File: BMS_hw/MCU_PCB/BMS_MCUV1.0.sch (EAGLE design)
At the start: 49 parts, among them IC2 SST25VF020B804ISA, J1 22-27-2051-05, J2 22-27-2051-05, J3 22-27-2041-04, J4 22-27-2051-05, U1 NCP1117LP-PG, X1 87758-2016

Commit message: Testing git bash trial !
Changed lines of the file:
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@@
 </instance>
 <instance part="X3" gate="-10" x="109.22" y="231.14" rot="R180">
-<attribute name="NAME" x="106.68" y="231.902" size="1.524" layer="95" rot="R180"/>
+<attribute name="NAME" x="99.06" y="236.982" size="1.524" layer="95" rot="R180"/>
 </instance>
 </instances>

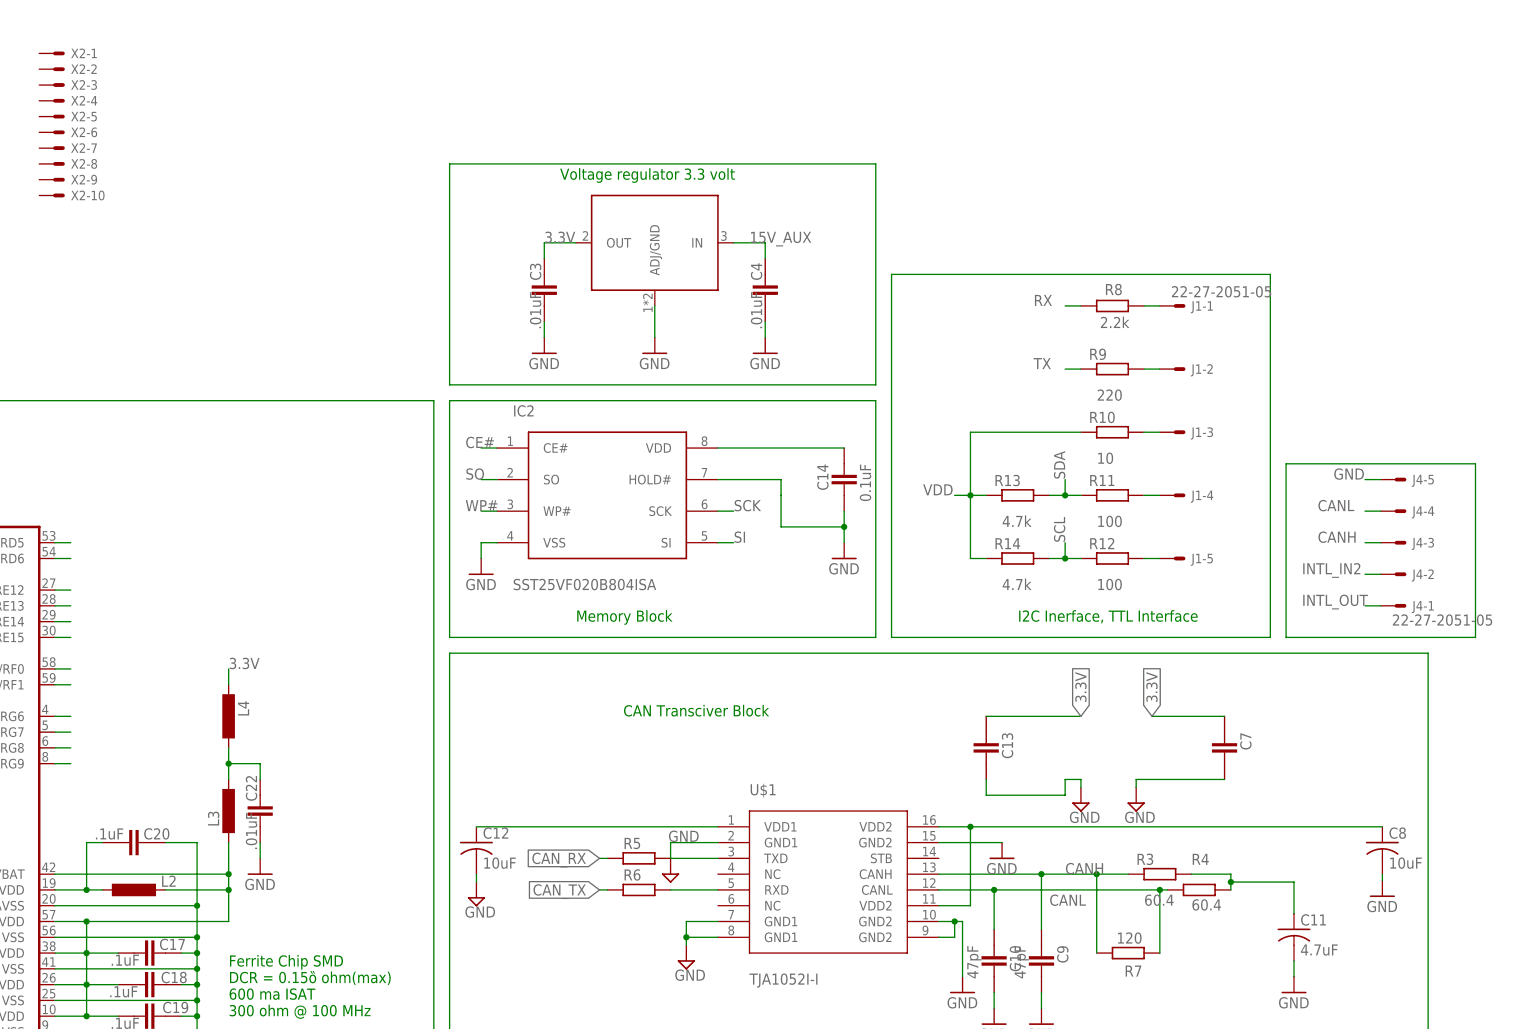
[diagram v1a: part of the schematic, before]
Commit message: updated schematic inductor part no 3.3 5v ldo net naaming
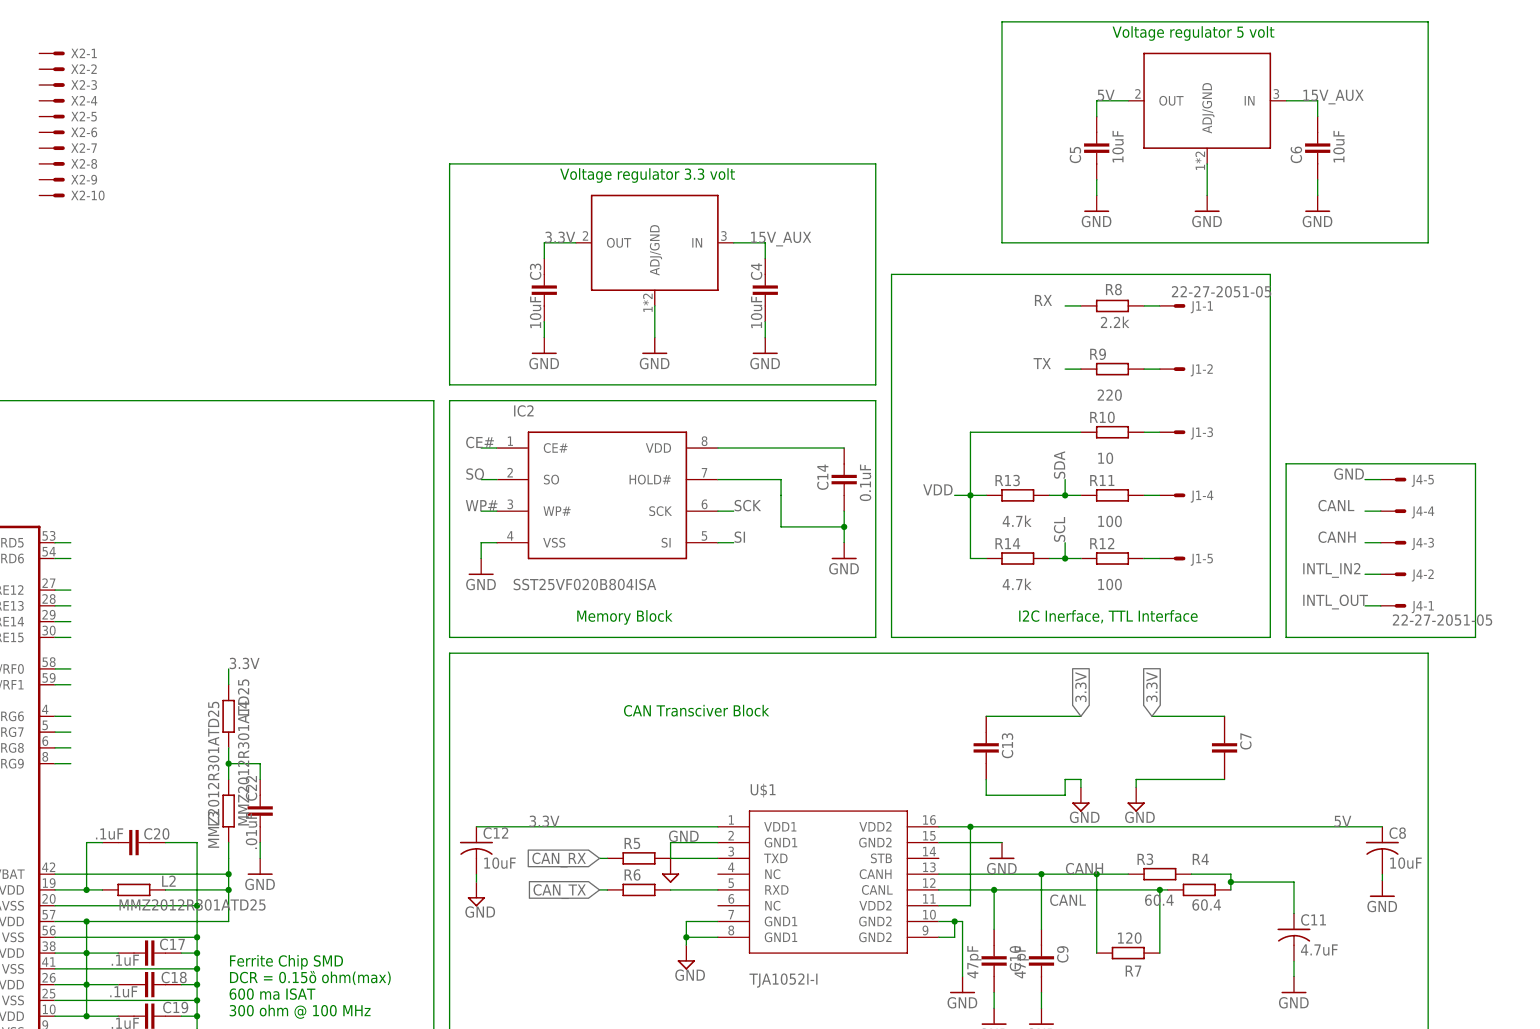
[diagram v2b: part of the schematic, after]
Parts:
- added C5, C6: 10uF, ipc-7351-capacitor:CAPACITOR_0603
- added U2: NCP1117LP-PG, GreenFuel:NCP1117LP-PG
- C3, C4: value .01uF -> 10uF
- L2, L3, L4: value (none) -> MMZ2012R301ATD25; device ipc-7351-inductor:INDUCTOR_0603 -> ipc-7351-resistor:RESISTOR_0805
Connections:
- removed net N$12: C8.1, U$1.VDD2, U$1.VDD2@1
- removed net N$8: C12.1, U$1.VDD1
- new net 5V: C5.2, C8.1, U$1.VDD2, U$1.VDD2@1, U2.OUT
- net 15V_AUX: now also C6.2, U2.IN
- net 3.3V: now also C12.1, U$1.VDD1
- net GND: now also C5.1, C6.1, U2.ADJ/GND
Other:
- note added: "Voltage regulator 5 volt"
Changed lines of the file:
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@@
 <part name="C19" library="ipc-7351-capacitor" deviceset="CAPACITOR_" device="0603" value=".1uF"/>
 <part name="GND21" library="supply1" library_urn="urn:adsk.eagle:library:371" deviceset="GND" device=""/>
-<part name="L2" library="ipc-7351-inductor" deviceset="INDUCTOR_" device="0603"/>
+<part name="L2" library="ipc-7351-resistor" deviceset="RESISTOR_" device="0805" value="MMZ2012R301ATD25"/>
 <part name="C20" library="ipc-7351-capacitor" deviceset="CAPACITOR_" device="0603" value=".1uF"/>
 <part name="R15" library="ipc-7351-resistor" deviceset="RESISTOR_" device="0603" value="1k"/>
@@
 <part name="C21" library="ipc-7351-capacitor" deviceset="CAPACITOR_" device="0603" value="0.1uF"/>
 <part name="GND22" library="supply1" library_urn="urn:adsk.eagle:library:371" deviceset="GND" device=""/>
-<part name="L3" library="ipc-7351-inductor" deviceset="INDUCTOR_" device="0603"/>
-<part name="L4" library="ipc-7351-inductor" deviceset="INDUCTOR_" device="0603"/>
+<part name="L3" library="ipc-7351-resistor" deviceset="RESISTOR_" device="0805" value="MMZ2012R301ATD25"/>
+<part name="L4" library="ipc-7351-resistor" deviceset="RESISTOR_" device="0805" value="MMZ2012R301ATD25"/>
 <part name="C22" library="ipc-7351-capacitor" deviceset="CAPACITOR_" device="0603" value=".01uF"/>
 <part name="GND23" library="supply1" library_urn="urn:adsk.eagle:library:371" deviceset="GND" device=""/>
 <part name="U1" library="GreenFuel" deviceset="NCP1117LP" device="-PG"/>
 <part name="GND3" library="supply1" library_urn="urn:adsk.eagle:library:371" deviceset="GND" device=""/>
-<part name="C3" library="ipc-7351-capacitor" deviceset="CAPACITOR_" device="0603" value=".01uF"/>
-<part name="C4" library="ipc-7351-capacitor" deviceset="CAPACITOR_" device="0603" value=".01uF"/>
+<part name="C3" library="ipc-7351-capacitor" deviceset="CAPACITOR_" device="0603" value="10uF"/>
+<part name="C4" library="ipc-7351-capacitor" deviceset="CAPACITOR_" device="0603" value="10uF"/>
 <part name="GND4" library="supply1" library_urn="urn:adsk.eagle:library:371" deviceset="GND" device=""/>
 <part name="GND5" library="supply1" library_urn="urn:adsk.eagle:library:371" deviceset="GND" device=""/>
@@
 <part name="X2" library="con-molex" library_urn="urn:adsk.eagle:library:165" deviceset="KK-156-10" device=""/>
 <part name="X3" library="con-molex" library_urn="urn:adsk.eagle:library:165" deviceset="KK-156-10" device=""/>
+<part name="U2" library="GreenFuel" deviceset="NCP1117LP" device="-PG"/>
+<part name="GND6" library="supply1" library_urn="urn:adsk.eagle:library:371" deviceset="GND" device=""/>
+<part name="C5" library="ipc-7351-capacitor" deviceset="CAPACITOR_" device="0603" value="10uF"/>
+<part name="C6" library="ipc-7351-capacitor" deviceset="CAPACITOR_" device="0603" value="10uF"/>
+<part name="GND7" library="supply1" library_urn="urn:adsk.eagle:library:371" deviceset="GND" device=""/>
+<part name="GND8" library="supply1" library_urn="urn:adsk.eagle:library:371" deviceset="GND" device=""/>
 </parts>
 <sheets>
@@
 <text x="233.68" y="210.82" size="1.778" layer="91">Voltage regulator 3.3 volt</text>
 <text x="289.56" y="12.7" size="2.1844" layer="94">Greenfuel Energy Solutions Pvt. Ltd.</text>
+<text x="322.58" y="233.68" size="1.778" layer="91">Voltage regulator 5 volt</text>
 </plain>
 <instances>
@@
 <instance part="X3" gate="-10" x="109.22" y="231.14" rot="R180">
 <attribute name="NAME" x="99.06" y="236.982" size="1.524" layer="95" rot="R180"/>
+</instance>
+<instance part="U2" gate="G$1" x="337.82" y="223.52"/>
+<instance part="GND6" gate="1" x="337.82" y="205.74">
+<attribute name="VALUE" x="335.28" y="203.2" size="1.778" layer="96"/>
+</instance>
+<instance part="C5" gate="G$1" x="320.04" y="215.9" rot="R90">
+<attribute name="NAME" x="317.5" y="213.36" size="1.778" layer="95" rot="R90"/>
+<attribute name="VALUE" x="324.358" y="213.36" size="1.778" layer="96" rot="R90"/>
+</instance>
+<instance part="C6" gate="G$1" x="355.6" y="215.9" rot="R90">
+<attribute name="NAME" x="353.06" y="213.36" size="1.778" layer="95" rot="R90"/>
+<attribute name="VALUE" x="359.918" y="213.36" size="1.778" layer="96" rot="R90"/>
+</instance>
+<instance part="GND7" gate="1" x="355.6" y="205.74">
+<attribute name="VALUE" x="353.06" y="203.2" size="1.778" layer="96"/>
+</instance>
+<instance part="GND8" gate="1" x="320.04" y="205.74">
+<attribute name="VALUE" x="317.5" y="203.2" size="1.778" layer="96"/>
 </instance>
 </instances>
@@
 <wire x1="326.39" y1="114.3" x2="340.614" y2="114.3" width="0.1524" layer="91"/>
 </segment>
+<segment>
+<pinref part="GND8" gate="1" pin="GND"/>
+<pinref part="C5" gate="G$1" pin="1"/>
+<wire x1="320.04" y1="208.28" x2="320.04" y2="210.82" width="0.1524" layer="91"/>
+</segment>
+<segment>
+<pinref part="GND7" gate="1" pin="GND"/>
+<pinref part="C6" gate="G$1" pin="1"/>
+<wire x1="355.6" y1="208.28" x2="355.6" y2="210.82" width="0.1524" layer="91"/>
+</segment>
+<segment>
+<pinref part="GND6" gate="1" pin="GND"/>
+<pinref part="U2" gate="G$1" pin="ADJ/GND"/>
+<wire x1="337.82" y1="208.28" x2="337.82" y2="213.36" width="0.1524" layer="91"/>
+</segment>
 </net>
 <net name="N$1" class="0">
@@
 <label x="180.34" y="132.08" size="1.778" layer="95"/>
 </segment>
+<segment>
+<pinref part="C12" gate="G$1" pin="1"/>
+<wire x1="220.218" y1="106.68" x2="259.08" y2="106.68" width="0.1524" layer="91"/>
+<pinref part="U$1" gate="G$1" pin="VDD1"/>
+<label x="228.6" y="106.68" size="1.778" layer="95"/>
+</segment>
 </net>
 <net name="N$6" class="0">
@@
 <wire x1="251.46" y1="101.6" x2="259.08" y2="101.6" width="0.1524" layer="91"/>
 <pinref part="U$1" gate="G$1" pin="TXD"/>
-</segment>
-</net>
-<net name="N$8" class="0">
-<segment>
-<pinref part="C12" gate="G$1" pin="1"/>
-<wire x1="220.218" y1="106.68" x2="259.08" y2="106.68" width="0.1524" layer="91"/>
-<pinref part="U$1" gate="G$1" pin="VDD1"/>
 </segment>
 </net>
@@
 <wire x1="351.79" y1="97.79" x2="341.63" y2="97.79" width="0.1524" layer="91"/>
 <junction x="341.63" y="97.79"/>
-</segment>
-</net>
-<net name="N$12" class="0">
-<segment>
-<pinref part="U$1" gate="G$1" pin="VDD2@1"/>
-<wire x1="294.64" y1="106.68" x2="299.72" y2="106.68" width="0.1524" layer="91"/>
-<pinref part="C8" gate="G$1" pin="1"/>
-<pinref part="U$1" gate="G$1" pin="VDD2"/>
-<wire x1="299.72" y1="106.68" x2="366.014" y2="106.68" width="0.1524" layer="91"/>
-<wire x1="294.64" y1="93.98" x2="299.72" y2="93.98" width="0.1524" layer="91"/>
-<wire x1="299.72" y1="93.98" x2="299.72" y2="106.68" width="0.1524" layer="91"/>
-<junction x="299.72" y="106.68"/>
 </segment>
 </net>
@@
 <label x="264.16" y="200.66" size="1.778" layer="95"/>
 </segment>
+<segment>
+<pinref part="U2" gate="G$1" pin="IN"/>
+<wire x1="350.52" y1="223.52" x2="355.6" y2="223.52" width="0.1524" layer="91"/>
+<pinref part="C6" gate="G$1" pin="2"/>
+<wire x1="355.6" y1="223.52" x2="355.6" y2="220.98" width="0.1524" layer="91"/>
+<label x="353.06" y="223.52" size="1.778" layer="95"/>
+</segment>
 </net>
 <net name="D_FET" class="0">
@@
 </segment>
 </net>
+<net name="N$17" class="0">
+<segment>
+<wire x1="304.8" y1="200.66" x2="304.8" y2="236.22" width="0.1524" layer="91"/>
+<wire x1="304.8" y1="236.22" x2="373.38" y2="236.22" width="0.1524" layer="91"/>
+<wire x1="373.38" y1="236.22" x2="373.38" y2="200.66" width="0.1524" layer="91"/>
+<wire x1="373.38" y1="200.66" x2="304.8" y2="200.66" width="0.1524" layer="91"/>
+</segment>
+</net>
+<net name="5V" class="0">
+<segment>
+<pinref part="U2" gate="G$1" pin="OUT"/>
+<pinref part="C5" gate="G$1" pin="2"/>
+<wire x1="325.12" y1="223.52" x2="320.04" y2="223.52" width="0.1524" layer="91"/>
+<wire x1="320.04" y1="223.52" x2="320.04" y2="220.98" width="0.1524" layer="91"/>
+<label x="320.04" y="223.52" size="1.778" layer="95"/>
+</segment>
+<segment>
+<pinref part="U$1" gate="G$1" pin="VDD2@1"/>
+<wire x1="294.64" y1="106.68" x2="299.72" y2="106.68" width="0.1524" layer="91"/>
+<pinref part="C8" gate="G$1" pin="1"/>
+<pinref part="U$1" gate="G$1" pin="VDD2"/>
+<wire x1="299.72" y1="106.68" x2="366.014" y2="106.68" width="0.1524" layer="91"/>
+<wire x1="294.64" y1="93.98" x2="299.72" y2="93.98" width="0.1524" layer="91"/>
+<wire x1="299.72" y1="93.98" x2="299.72" y2="106.68" width="0.1524" layer="91"/>
+<junction x="299.72" y="106.68"/>
+<label x="358.14" y="106.68" size="1.778" layer="95"/>
+</segment>
+</net>

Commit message: hjhk
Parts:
- removed X1: 87758-2016, con-molex:87758-2016
- removed X2, X3: (no value), con-molex:KK-156-10
- added JP1, JP5: (no value), GreenFuel:PINHD-1X15
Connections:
- net 15V_AUX: no longer X1-17.S
- net C_FET: no longer X1-9.S
- net D_FET: no longer X1-19.S
- net FAULT: no longer X1-5.S
- net GND: no longer U$1.GND1, X1-1.S, X1-10.S, X1-14.S, X1-15.S, X1-16.S, X1-18.S, X1-2.S, X1-20.S, X1-3.S, X1-6.S, X1-7.S, X1-8.S
- net ISP: no longer X1-11.S
- net N$7: now also U$1.GND1
- net PCHG_FET: no longer X1-4.S
- net VDD: no longer X1-12.S, X1-13.S
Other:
- moved on the sheet: C1, C17, C18, C19, C2, C20, C21, C22, L2, L3, L4, MCU2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

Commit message: asdasd
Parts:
- C1, C2, C21: device ipc-7351-capacitor:CAPACITOR_0603 -> ipc-7351-capacitor:CAPACITOR_0402
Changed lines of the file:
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@@
 <parts>
 <part name="Q1" library="adafruit" deviceset="CRYSTAL" device="CTS406"/>
-<part name="C1" library="ipc-7351-capacitor" deviceset="CAPACITOR_" device="0603" value="20pF"/>
-<part name="C2" library="ipc-7351-capacitor" deviceset="CAPACITOR_" device="0603" value="20pF"/>
+<part name="C1" library="ipc-7351-capacitor" deviceset="CAPACITOR_" device="0402" value="20pF"/>
+<part name="C2" library="ipc-7351-capacitor" deviceset="CAPACITOR_" device="0402" value="20pF"/>
 <part name="GND1" library="supply1" library_urn="urn:adsk.eagle:library:371" deviceset="GND" device=""/>
 <part name="GND2" library="supply1" library_urn="urn:adsk.eagle:library:371" deviceset="GND" device=""/>
@@
 <part name="R15" library="ipc-7351-resistor" deviceset="RESISTOR_" device="0603" value="1k"/>
 <part name="R16" library="ipc-7351-resistor" deviceset="RESISTOR_" device="0603" value="10k"/>
-<part name="C21" library="ipc-7351-capacitor" deviceset="CAPACITOR_" device="0603" value="0.1uF"/>
+<part name="C21" library="ipc-7351-capacitor" deviceset="CAPACITOR_" device="0402" value="0.1uF"/>
 <part name="GND22" library="supply1" library_urn="urn:adsk.eagle:library:371" deviceset="GND" device=""/>
 <part name="L3" library="ipc-7351-resistor" deviceset="RESISTOR_" device="0805" value="MMZ2012R301ATD25"/>

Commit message: brd layout and sch updated!
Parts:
- C10, C13, C7, C9: device ipc-7351-capacitor:CAPACITOR_0805 -> ipc-7351-capacitor:CAPACITOR_0402
- C11, C12, C8: device adafruit:C-USC0805 -> ipc-7351-capacitor:CAPACITOR_0402
- C14, C17, C18, C19, C20, C22, C3, C4: device ipc-7351-capacitor:CAPACITOR_0603 -> ipc-7351-capacitor:CAPACITOR_0402
- Q1: value (none) -> CRYSTALS-GND-LID-IQXC-42; device adafruit:CRYSTALCTS406 -> IQD-Frequency-Products:CRYSTALS-GND-LID-IQXC-42
- R10, R11, R12, R13, R14, R3, R4, R5, R6, R7, R8, R9: device ipc-7351-resistor:RESISTOR_0805 -> ipc-7351-resistor:RESISTOR_0402
- R15, R16: device ipc-7351-resistor:RESISTOR_0603 -> ipc-7351-resistor:RESISTOR_0402
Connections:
- new net N$3: C12.1, U$1.VDD1
- net 3.3V: no longer C12.1, U$1.VDD1
- net GND: now also Q1.2, Q1.4
- net N$1: now also Q1.3; no longer Q1.2
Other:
- moved on the sheet: C1, C11, C12, C2, C8

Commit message: board layout and schematic files updated@12
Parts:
- removed C3, C4: 10uF, ipc-7351-capacitor:CAPACITOR_0402
- removed C5, C6: 10uF, ipc-7351-capacitor:CAPACITOR_0603
- removed J1, J2, J4: 22-27-2051-05, con-molex:22-27-2051-05
- removed J3: 22-27-2041-04, con-molex:22-27-2041-04
- removed U1, U2: NCP1117LP-PG, GreenFuel:NCP1117LP-PG
- added JP2: (no value), GreenFuel:PINHD-1X12
- Q1: device IQD-Frequency-Products:CRYSTALS-GND-LID-IQXC-42 -> GreenFuel:CRYSTALS-GND-LID-IQXC-42
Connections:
- removed net 15V_AUX: C4.2, C6.2, U1.IN, U2.IN
- removed net N$18: J1-1.S, R8.2
- removed net N$19: J1-2.S, R9.2
- removed net N$20: J1-3.S, R10.2
- removed net N$21: J1-4.S, R11.2
- removed net N$22: J1-5.S, R12.2
- removed net VSS: J2-3.S
- net !MCLR: no longer J2-1.S
- net 3.3V: no longer C3.2, U1.OUT
- net 5V: no longer C5.2, U2.OUT
- net CANH: no longer J4-3.S
- net CANL: no longer J4-4.S
- net DBG_RX: no longer J3-3.S
- net DBG_TX: no longer J3-2.S
- net GND: no longer C3.1, C4.1, C5.1, C6.1, J3-1.S, J3-4.S, J4-5.S, U1.ADJ/GND, U2.ADJ/GND
- net ICSPCLK: no longer J2-5.S
- net ICSPDAT: no longer J2-4.S
- net INTL_IN2: no longer J4-2.S
- net INTL_OUT: no longer J4-1.S
- net VDD: no longer J2-2.S
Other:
- note removed: "Note : Temperature sense"
- note removed: "Note: Programmer"
- note removed: "Voltage regulator 3.3 volt"
- note removed: "Voltage regulator 5 volt"
- moved on the sheet: JP1
